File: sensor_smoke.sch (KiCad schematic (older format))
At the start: 15 parts, among them U501 TLV70018, U502 ADPD188BI, U503 Smoke Chamber

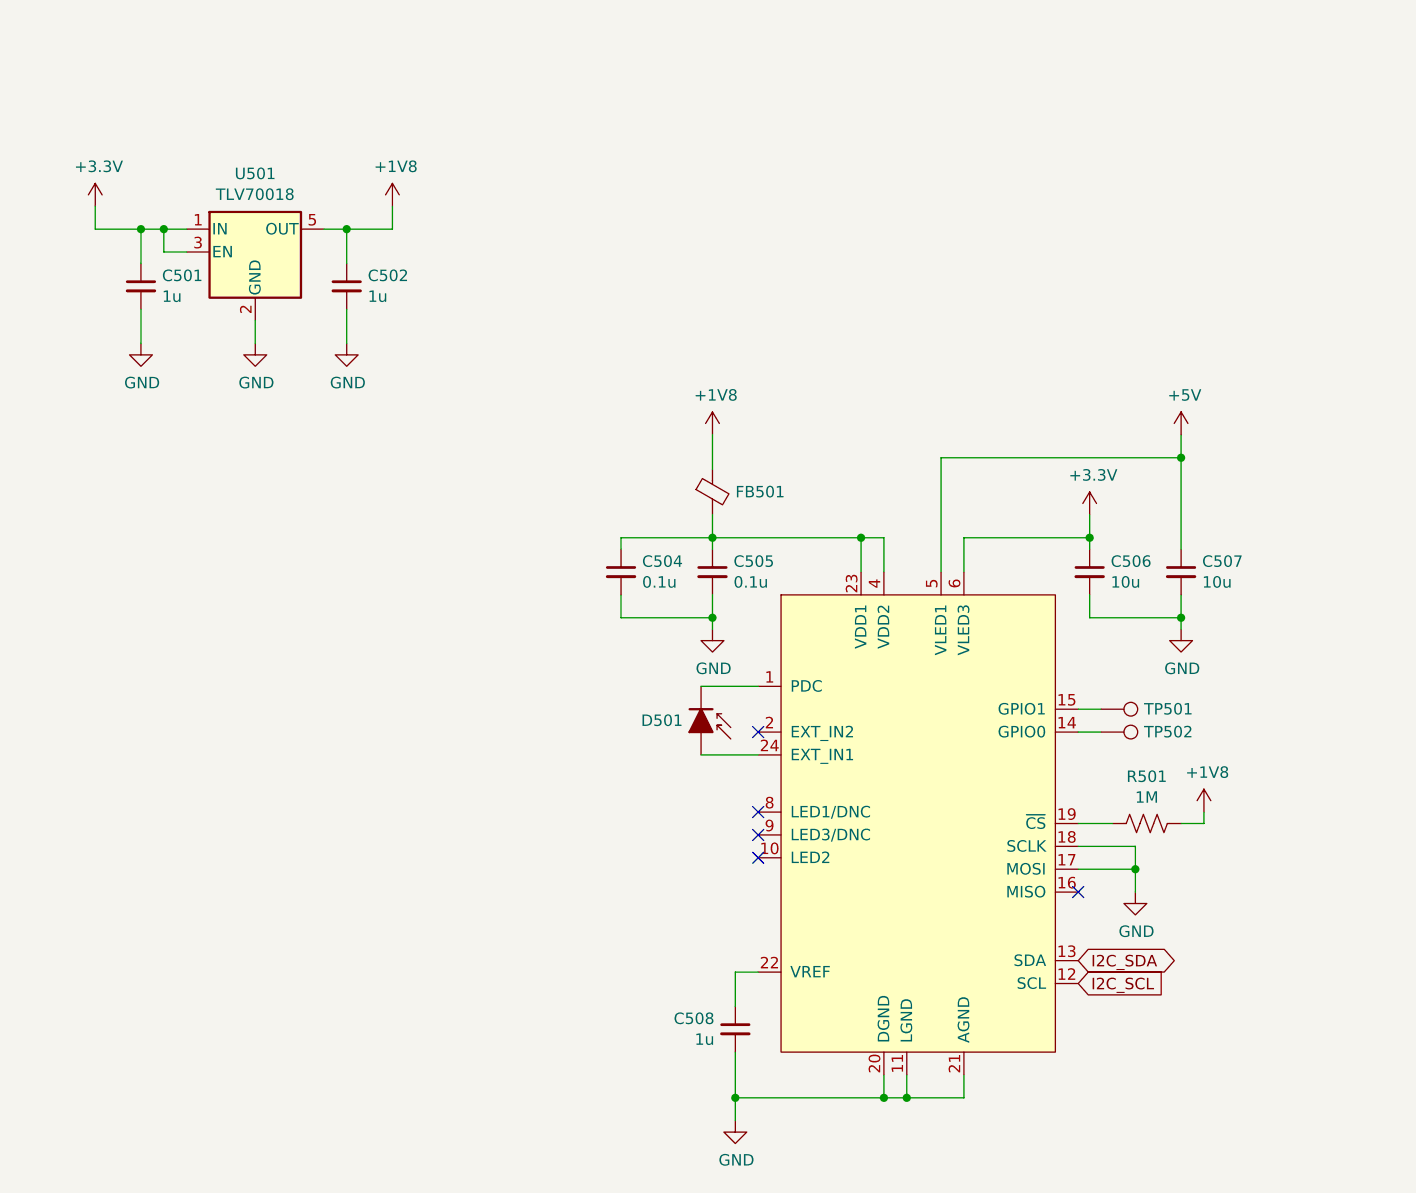
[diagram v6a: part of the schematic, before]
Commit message: Re-annotate all parts
Cleans up annotations
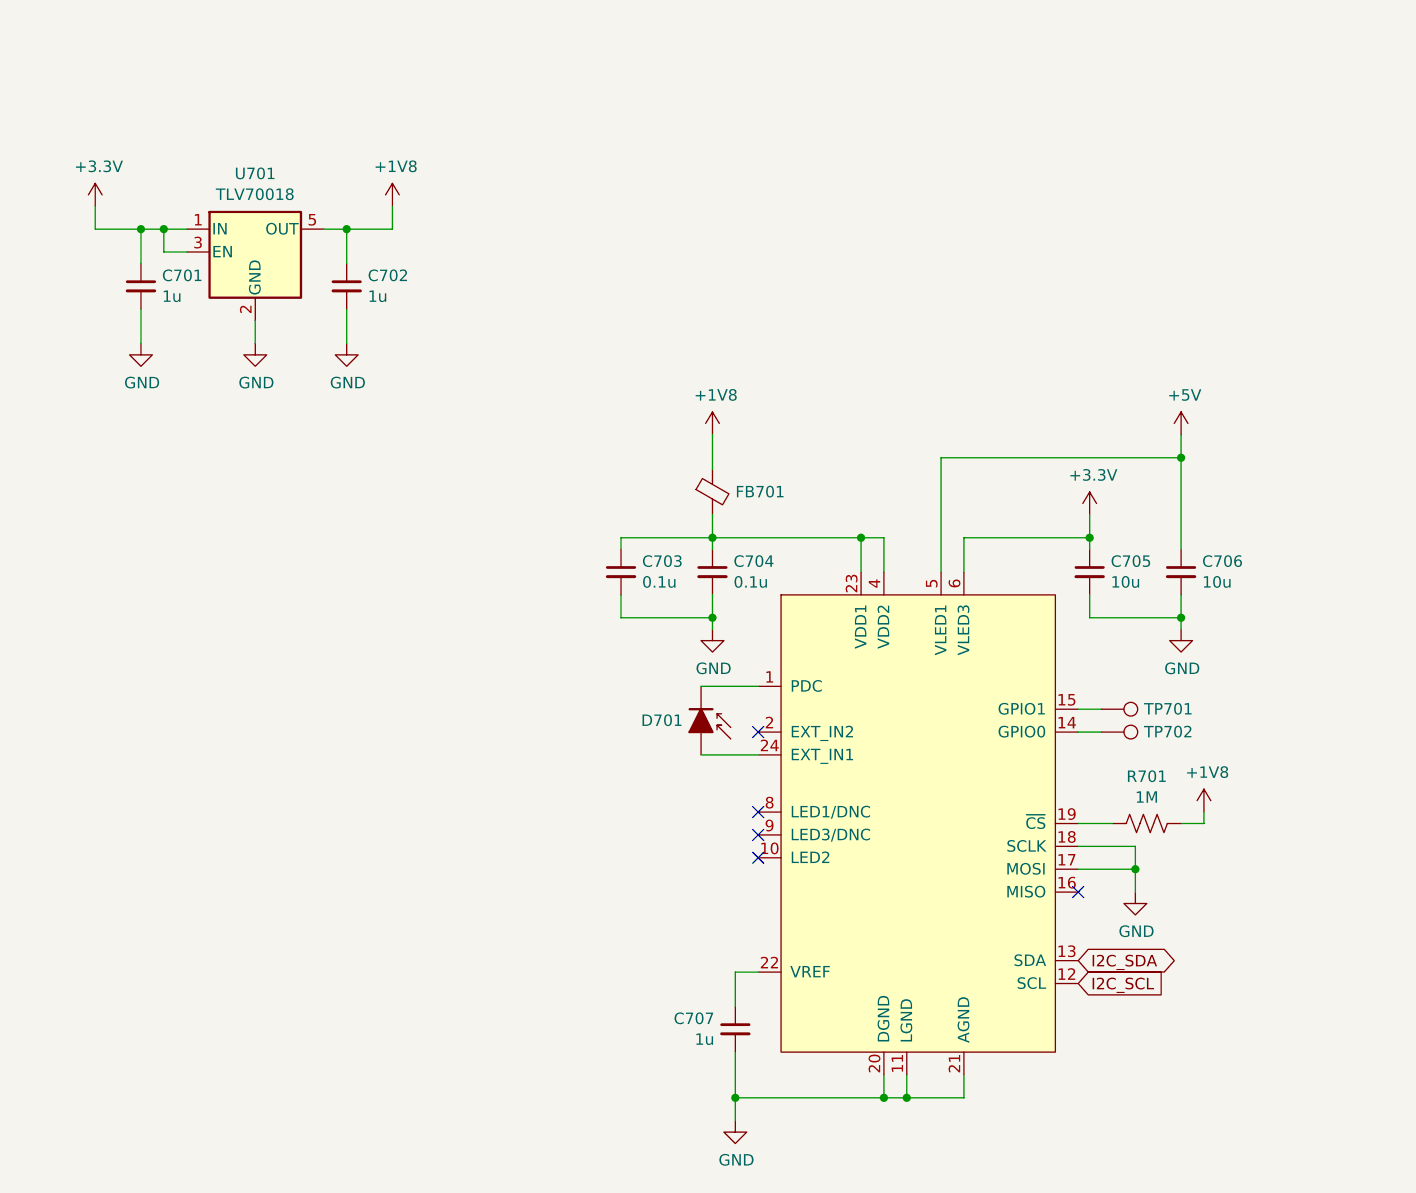
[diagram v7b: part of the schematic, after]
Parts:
- renumbered C501 to C701, C502 to C702, C504 to C703, C505 to C704, C506 to C705, C507 to C706, C508 to C707, D501 to D701, FB501 to FB701, R501 to R701, TP501 to TP701, TP502 to TP702, U501 to U701, U502 to U702, U503 to U703
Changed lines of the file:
@@
 SERCOM 0
 $Comp
-L mylib:ADPD188BI U502
+L mylib:ADPD188BI U?
 U 1 1 5FA33904
 P 5400 4350
-AR Path="/5FA33904" Ref="U502"  Part="1"
-AR Path="/5F9DB5BA/5FA33904" Ref="U502"  Part="1"
-F 0 "U502" H 5350 3361 50  0001 C CNN
+AR Path="/5FA33904" Ref="U?"  Part="1"
+AR Path="/5F9DB5BA/5FA33904" Ref="U702"  Part="1"
+F 0 "U702" H 5350 3361 50  0001 C CNN
 F 1 "ADPD188BI" H 5350 3270 50  0001 C CNN
 F 2 "mylib:ADPD188BI" H 4750 4000 50  0001 C CNN
@@
 $EndComp
 $Comp
-L power:GND #PWR0514
+L power:GND #PWR0713
 U 1 1 5FA38307
 P 4600 5500
-F 0 "#PWR0514" H 4600 5250 50  0001 C CNN
+F 0 "#PWR0713" H 4600 5250 50  0001 C CNN
 F 1 "GND" H 4605 5327 50  0000 C CNN
 F 2 "" H 4600 5500 50  0001 C CNN
@@
 $EndComp
 $Comp
-L Device:Ferrite_Bead_Small FB501
+L Device:Ferrite_Bead_Small FB701
 U 1 1 5FA39D74
 P 4500 2750
-F 0 "FB501" H 4600 2750 50  0000 L CNN
+F 0 "FB701" H 4600 2750 50  0000 L CNN
 F 1 "Ferrite_Bead_Small" H 4600 2705 50  0001 L CNN
 F 2 "Inductor_SMD:L_0603_1608Metric" V 4430 2750 50  0001 C CNN
@@
 Connection ~ 5150 2950
 $Comp
-L power:GND #PWR0510
+L power:GND #PWR0709
 U 1 1 5FA3D3A1
 P 4500 3350
-F 0 "#PWR0510" H 4500 3100 50  0001 C CNN
+F 0 "#PWR0709" H 4500 3100 50  0001 C CNN
 F 1 "GND" H 4505 3177 50  0000 C CNN
 F 2 "" H 4500 3350 50  0001 C CNN
@@
 I2C_SCL
 $Comp
-L Regulator_Linear:TLV70018_SOT23-5 U501
+L Regulator_Linear:TLV70018_SOT23-5 U701
 U 1 1 5FA5D12F
 P 2500 1700
-F 0 "U501" H 2500 2042 50  0000 C CNN
+F 0 "U701" H 2500 2042 50  0000 C CNN
 F 1 "TLV70018" H 2500 1951 50  0000 C CNN
 F 2 "Package_TO_SOT_SMD:SOT-353_SC-70-5" H 2500 2025 50  0001 C CIN
@@
 $EndComp
 $Comp
-L power:+3.3V #PWR0501
+L power:+3.3V #PWR0701
 U 1 1 5FA60D6A
 P 1800 1500
-F 0 "#PWR0501" H 1800 1350 50  0001 C CNN
+F 0 "#PWR0701" H 1800 1350 50  0001 C CNN
 F 1 "+3.3V" H 1815 1673 50  0000 C CNN
 F 2 "" H 1800 1500 50  0001 C CNN
@@
 	2100 1600 2200 1600
 $Comp
-L power:GND #PWR0504
+L power:GND #PWR0704
 U 1 1 5FA62FF8
 P 2500 2100
-F 0 "#PWR0504" H 2500 1850 50  0001 C CNN
+F 0 "#PWR0704" H 2500 1850 50  0001 C CNN
 F 1 "GND" H 2505 1927 50  0000 C CNN
 F 2 "" H 2500 2100 50  0001 C CNN
@@
 	2500 2100 2500 2000
 $Comp
-L power:GND #PWR0503
+L power:GND #PWR0703
 U 1 1 5FA6430A
 P 2000 2100
-F 0 "#PWR0503" H 2000 1850 50  0001 C CNN
+F 0 "#PWR0703" H 2000 1850 50  0001 C CNN
 F 1 "GND" H 2005 1927 50  0000 C CNN
 F 2 "" H 2000 2100 50  0001 C CNN
@@
 $EndComp
 $Comp
-L power:GND #PWR0505
+L power:GND #PWR0705
 U 1 1 5FA64654
 P 2900 2100
-F 0 "#PWR0505" H 2900 1850 50  0001 C CNN
+F 0 "#PWR0705" H 2900 1850 50  0001 C CNN
 F 1 "GND" H 2905 1927 50  0000 C CNN
 F 2 "" H 2900 2100 50  0001 C CNN
@@
 $EndComp
 $Comp
-L power:+1V8 #PWR0502
+L power:+1V8 #PWR0702
 U 1 1 5FA659F5
 P 3100 1500
-F 0 "#PWR0502" H 3100 1350 50  0001 C CNN
+F 0 "#PWR0702" H 3100 1350 50  0001 C CNN
 F 1 "+1V8" H 3115 1673 50  0000 C CNN
 F 2 "" H 3100 1500 50  0001 C CNN
@@
 	5500 2600 5500 3100
 $Comp
-L power:GND #PWR0513
+L power:GND #PWR0712
 U 1 1 5FA91B81
 P 6350 4500
-F 0 "#PWR0513" H 6350 4250 50  0001 C CNN
+F 0 "#PWR0712" H 6350 4250 50  0001 C CNN
 F 1 "GND" H 6355 4327 50  0000 C CNN
 F 2 "" H 6350 4500 50  0001 C CNN
@@
 AR Path="/5E5C8043/5EAB3002/5FAA30B6" Ref="C?"  Part="1"
 AR Path="/5E5C8043/5FAA30B6" Ref="C?"  Part="1"
-AR Path="/5F9DB5BA/5FAA30B6" Ref="C501"  Part="1"
-F 0 "C501" H 1908 1896 50  0000 R CNN
+AR Path="/5F9DB5BA/5FAA30B6" Ref="C701"  Part="1"
+F 0 "C701" H 1908 1896 50  0000 R CNN
 F 1 "1u" H 1908 1805 50  0000 R CNN
 F 2 "Capacitor_SMD:C_0603_1608Metric" H 2000 1850 50  0001 C CNN
@@
 AR Path="/5E5C8043/5EAB3002/5FAA41BF" Ref="C?"  Part="1"
 AR Path="/5E5C8043/5FAA41BF" Ref="C?"  Part="1"
-AR Path="/5F9DB5BA/5FAA41BF" Ref="C502"  Part="1"
-F 0 "C502" H 2808 1896 50  0000 R CNN
+AR Path="/5F9DB5BA/5FAA41BF" Ref="C702"  Part="1"
+F 0 "C702" H 2808 1896 50  0000 R CNN
 F 1 "1u" H 2808 1805 50  0000 R CNN
 F 2 "Capacitor_SMD:C_0603_1608Metric" H 2900 1850 50  0001 C CNN
@@
 AR Path="/5E5C8043/5EAB3002/5FAACFD7" Ref="C?"  Part="1"
 AR Path="/5E5C8043/5FAACFD7" Ref="C?"  Part="1"
-AR Path="/5F9DB5BA/5FAACFD7" Ref="C508"  Part="1"
-F 0 "C508" H 4691 5146 50  0000 L CNN
+AR Path="/5F9DB5BA/5FAACFD7" Ref="C707"  Part="1"
+F 0 "C707" H 4691 5146 50  0000 L CNN
 F 1 "1u" H 4691 5055 50  0000 L CNN
 F 2 "Capacitor_SMD:C_0603_1608Metric" H 4600 5100 50  0001 C CNN
@@
 	4450 3600 4700 3600
 $Comp
-L Connector:TestPoint TP501
+L Connector:TestPoint TP701
 U 1 1 5FAF5131
 P 6200 3700
-F 0 "TP501" V 6200 3888 50  0000 L CNN
+F 0 "TP701" V 6200 3888 50  0000 L CNN
 F 1 "TestPoint" V 6096 3772 50  0001 C CNN
 F 2 "TestPoint:TestPoint_Pad_D1.0mm" H 6400 3700 50  0001 C CNN
@@
 $EndComp
 $Comp
-L Connector:TestPoint TP502
+L Connector:TestPoint TP702
 U 1 1 5FAF78A5
 P 6200 3800
-F 0 "TP502" V 6200 3988 50  0000 L CNN
+F 0 "TP702" V 6200 3988 50  0000 L CNN
 F 1 "TestPoint" V 6245 3988 50  0001 L CNN
 F 2 "TestPoint:TestPoint_Pad_D1.0mm" H 6400 3800 50  0001 C CNN
@@
 $EndComp
 $Comp
-L power:GND #PWR0511
+L power:GND #PWR0710
 U 1 1 5FAD064C
 P 6550 3350
-F 0 "#PWR0511" H 6550 3100 50  0001 C CNN
+F 0 "#PWR0710" H 6550 3100 50  0001 C CNN
 F 1 "GND" H 6555 3177 50  0000 C CNN
 F 2 "" H 6550 3350 50  0001 C CNN
@@
 P 6150 3100
 AR Path="/5FB2E92E" Ref="C?"  Part="1"
-AR Path="/5F9DB5BA/5FB2E92E" Ref="C506"  Part="1"
-F 0 "C506" H 6242 3146 50  0000 L CNN
+AR Path="/5F9DB5BA/5FB2E92E" Ref="C705"  Part="1"
+F 0 "C705" H 6242 3146 50  0000 L CNN
 F 1 "10u" H 6242 3055 50  0000 L CNN
 F 2 "Capacitor_SMD:C_0603_1608Metric" H 6150 3100 50  0001 C CNN
@@
 P 6550 3100
 AR Path="/5FB2D183" Ref="C?"  Part="1"
-AR Path="/5F9DB5BA/5FB2D183" Ref="C507"  Part="1"
-F 0 "C507" H 6642 3146 50  0000 L CNN
+AR Path="/5F9DB5BA/5FB2D183" Ref="C706"  Part="1"
+F 0 "C706" H 6642 3146 50  0000 L CNN
 F 1 "10u" H 6642 3055 50  0000 L CNN
 F 2 "Capacitor_SMD:C_0603_1608Metric" H 6550 3100 50  0001 C CNN
@@
 	6150 2850 6150 2950
 $Comp
-L power:+5V #PWR0507
+L power:+5V #PWR0707
 U 1 1 5FA8E43B
 P 6550 2500
-F 0 "#PWR0507" H 6550 2350 50  0001 C CNN
+F 0 "#PWR0707" H 6550 2350 50  0001 C CNN
 F 1 "+5V" H 6565 2673 50  0000 C CNN
 F 2 "" H 6550 2500 50  0001 C CNN
@@
 $EndComp
 $Comp
-L power:+3.3V #PWR0509
+L power:+3.3V #PWR0708
 U 1 1 5FA7F025
 P 6150 2850
-F 0 "#PWR0509" H 6150 2700 50  0001 C CNN
+F 0 "#PWR0708" H 6150 2700 50  0001 C CNN
 F 1 "+3.3V" H 6165 3023 50  0000 C CNN
 F 2 "" H 6150 2850 50  0001 C CNN
@@
 P 6400 4200
 AR Path="/5FB53BAA" Ref="R?"  Part="1"
-AR Path="/5F9DB5BA/5FB53BAA" Ref="R501"  Part="1"
-F 0 "R501" V 6605 4200 50  0000 C CNN
+AR Path="/5F9DB5BA/5FB53BAA" Ref="R701"  Part="1"
+F 0 "R701" V 6605 4200 50  0000 C CNN
 F 1 "1M" V 6514 4200 50  0000 C CNN
 F 2 "Resistor_SMD:R_0603_1608Metric" H 6400 4200 60  0001 C CNN
@@
 $EndComp
 $Comp
-L Device:D_Photo_ALT D501
+L Device:D_Photo_ALT D701
 U 1 1 5FB5BF5D
 P 4450 3800
-F 0 "D501" V 4400 3721 50  0000 R CNN
+F 0 "D701" V 4400 3721 50  0000 R CNN
 F 1 "Photodiode alt" V 4445 3720 50  0001 R CNN
 F 2 "LED_THT:LED_D3.0mm_Clear" H 4400 3800 50  0001 C CNN
@@
 	4500 2500 4500 2650
 $Comp
-L power:+1V8 #PWR0508
+L power:+1V8 #PWR0706
 U 1 1 5FA3944F
 P 4500 2500
-F 0 "#PWR0508" H 4500 2350 50  0001 C CNN
+F 0 "#PWR0706" H 4500 2350 50  0001 C CNN
 F 1 "+1V8" H 4515 2673 50  0000 C CNN
 F 2 "" H 4500 2500 50  0001 C CNN
@@
 AR Path="/5F9D72A5/5FAB0389" Ref="C?"  Part="1"
 AR Path="/5FCEDB09/5FAB0389" Ref="C?"  Part="1"
-AR Path="/5F9DB5BA/5FAB0389" Ref="C505"  Part="1"
-F 0 "C505" H 4592 3146 50  0000 L CNN
+AR Path="/5F9DB5BA/5FAB0389" Ref="C704"  Part="1"
+F 0 "C704" H 4592 3146 50  0000 L CNN
 F 1 "0.1u" H 4592 3055 50  0000 L CNN
 F 2 "Capacitor_SMD:C_0603_1608Metric" H 4500 3100 50  0001 C CNN
@@
 AR Path="/5F9D72A5/5FAB1576" Ref="C?"  Part="1"
 AR Path="/5FCEDB09/5FAB1576" Ref="C?"  Part="1"
-AR Path="/5F9DB5BA/5FAB1576" Ref="C504"  Part="1"
-F 0 "C504" H 4192 3146 50  0000 L CNN
+AR Path="/5F9DB5BA/5FAB1576" Ref="C703"  Part="1"
+F 0 "C703" H 4192 3146 50  0000 L CNN
 F 1 "0.1u" H 4192 3055 50  0000 L CNN
 F 2 "Capacitor_SMD:C_0603_1608Metric" H 4100 3100 50  0001 C CNN
@@
 	6650 4150 6650 4200
 $Comp
-L power:+1V8 #PWR0512
+L power:+1V8 #PWR0711
 U 1 1 5FA944B4
 P 6650 4150
-F 0 "#PWR0512" H 6650 4000 50  0001 C CNN
+F 0 "#PWR0711" H 6650 4000 50  0001 C CNN
 F 1 "+1V8" H 6665 4323 50  0000 C CNN
 F 2 "" H 6650 4150 50  0001 C CNN
@@
 	2900 1600 3100 1600
 $Comp
-L mylib:Chamber U503
+L mylib:Chamber U703
 U 1 1 5FB92C1C
 P 7800 6150
-F 0 "U503" H 7800 6465 50  0001 C CNN
+F 0 "U703" H 7800 6465 50  0001 C CNN
 F 1 "Smoke Chamber" H 8128 6200 50  0000 L CNN
 F 2 "mylib:ADPD188BI_Chamber" H 7800 6150 50  0001 C CNN

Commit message: BOM reduction and part picking
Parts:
- R701: LCSC (none) -> C105578
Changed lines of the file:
@@
 F 5 "RC0603FR-071ML" H 6400 4200 50  0001 C CNN "MPN"
 F 6 "RES SMD 1M OHM 1% 1/10W 0603" H 6400 4200 50  0001 C CNN "Note"
+F 7 "C105578" H 6400 4200 50  0001 C CNN "LCSC"
 	1    6400 4200
 	0    -1   -1   0
